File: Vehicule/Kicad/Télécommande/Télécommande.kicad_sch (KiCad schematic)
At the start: 1 part, among them U1 ESP32-C3_SUPERMINI

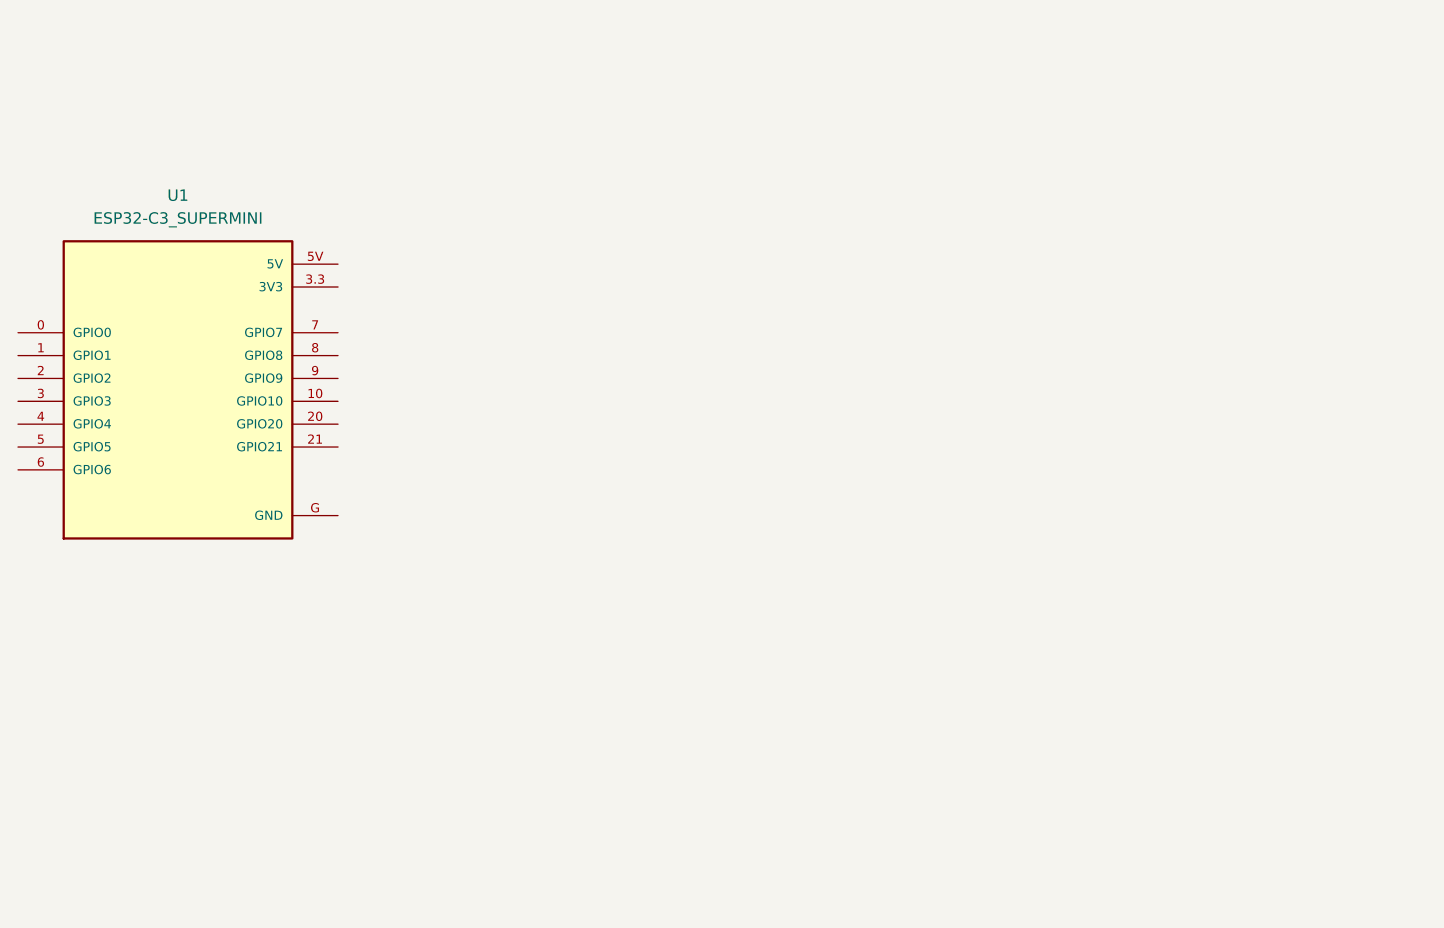
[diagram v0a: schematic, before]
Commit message: Création du joystick Ajout du joystick Ajout des trimmers
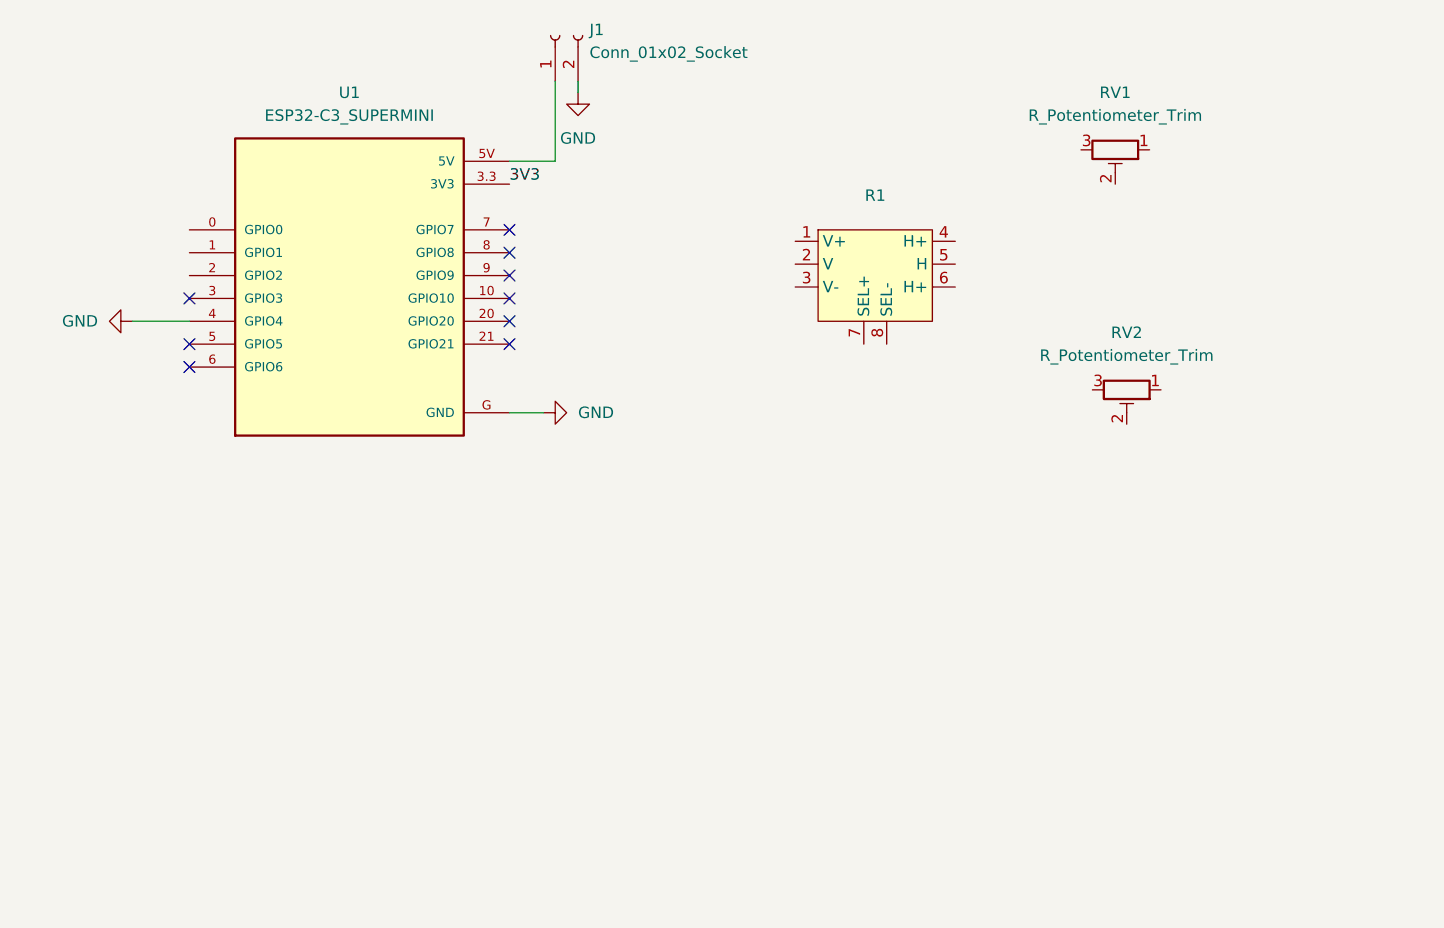
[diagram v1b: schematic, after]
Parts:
- added J1: Conn_01x02_Socket, symbol Connector:Conn_01x02_Socket
- added R1: ~, symbol Anumby:Joystick
- added RV1, RV2: R_Potentiometer_Trim, symbol Device:R_Potentiometer_Trim
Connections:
- net 3V3: now reaches U1.3.3 (3V3)
- net GND: now reaches U1.4 (GPIO4)
- net GND: now also U1.G (GND), J1.2 (Pin_2)
- net at U1.5V: now also J1.1 (Pin_1)
- no-connect marks 0 -> 9
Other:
- moved on the sheet: U1

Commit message: Création du joystick Ajout du joystick Ajout des trimmers
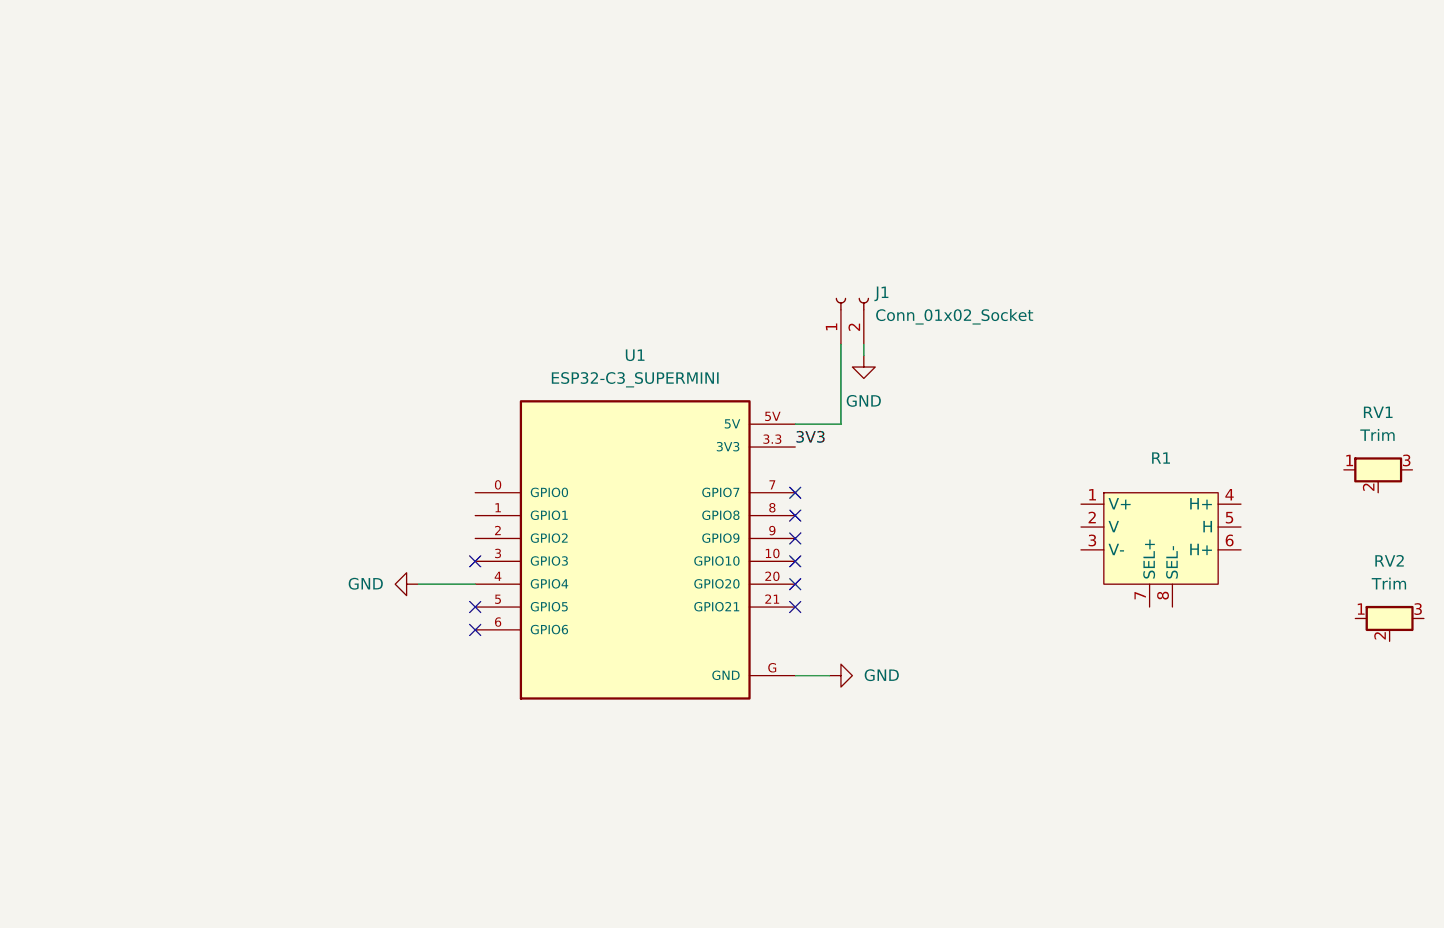
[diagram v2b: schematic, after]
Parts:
- removed RV1, RV2: R_Potentiometer_Trim, symbol Device:R_Potentiometer_Trim
- added RV1, RV2: Trim, symbol Anumby:Trimmer
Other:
- title: (none) -> Joystick
- moved on the sheet: J1, R1, U1

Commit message: Empeinte du joystick
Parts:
- R1: footprint (none) -> Empreintes:Joystick
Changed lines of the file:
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@@
 		(on_board yes)
 		(dnp no)
-		(fields_autoplaced yes)
 		(property "Reference" "R1"
 			(at 171.45 95.25 0)
@@
 			)
 		)
-		(property "Footprint" ""
-			(at 167.64 97.79 0)
+		(property "Footprint" "Empreintes:Joystick"
+			(at 170.942 97.282 0)
 			(effects
 				(font
 					(size 1.27 1.27)
 				)
-				(hide yes)
 			)
 		)

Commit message: Compléter le schéma
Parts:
- R1: footprint Empreintes:Joystick -> (none)
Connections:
- net 3V3: now also R1.8 (SEL-), RV1.1, RV2.3
- net GND: now also R1. (GND), R1.3 (V-), R1.4 (H+); no longer U1.4 (GPIO4)
- net at RV1.2: now also R1.1 (V+)
- net at RV2.2: now also R1.6 (H+)
- net at R1.2 (V): now also U1.5 (GPIO5)
- net at R1.5 (H): now also U1.6 (GPIO6)
- net at R1.7 (SEL+): now also U1.4 (GPIO4)
- net 5V: now reaches J1.1 (Pin_1), U1.5V
- no-connect marks 9 -> 12
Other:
- moved on the sheet: RV1, RV2, U1

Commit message: Compléter le schéma
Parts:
- U1: footprint ESP32-C3_SUPERMINI:MODULE_ESP32-C3_SUPERMINI -> ESP32-C3_SUPERMINI
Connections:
- no-connect marks 12 -> 15
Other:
- moved on the sheet: RV1, RV2
